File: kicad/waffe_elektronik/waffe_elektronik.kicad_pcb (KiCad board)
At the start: 4 copper layers, 59.6 x 51 mm, 81 parts, among them J1 WS2812 HP-Streifen, J2 GX16 7-polig, J3 USB-C (Flashen + Laden), J4 OLED I²C (Qwiic), J5 Drehgeber, J6 TSOP 6 (Waffe), J7 TF-018, M1 Vibromotor, Q1 AO3400A, Q2 AO3400A, Q3 FS8205A, SW1 Taster, SW2 Taster, SW3 RESET, SW4 BOOT, U1 MT3608, U12 USBLC6-2SC6, U14 GD5F1GQ5UEYIGR, U15 DW01A, U2 AMS1117-3.3, U3 MCP73831, U4 ESP32-S3-WROOM-1-N16R8, U5 74HCT125, U6 MAX98357A

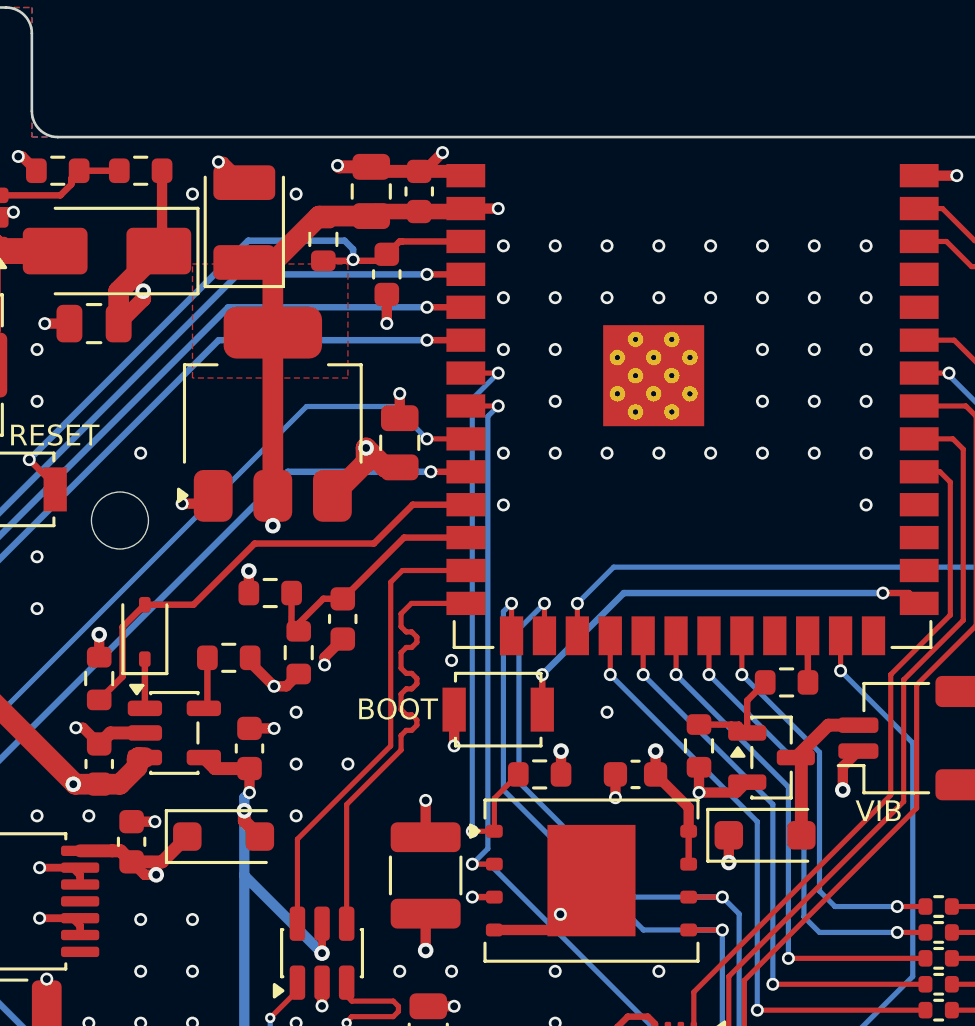
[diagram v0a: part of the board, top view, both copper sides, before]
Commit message: Platine: günstigere JLC-Teile, Option ESP32-S3-WROOM-1U mit externer Antenne
- Flash ZD35Q1GC-IB, Kondensatoren/Dioden/Widerstände auf Basic-Teile und 0402, Layout angepasst
- WROOM-1U auf demselben Footprint: eigene JLCPCB-BOM/CPL (Modulmitte 3,15 mm versetzt),
  Mouser-Option mit Pigtail RP-SMA/U.FL und Knick-Stabantenne, 3D-Modell des 1U
- Gerber, BOM, CPL, Renders und Bestelllisten neu erzeugt

Co-Authored-By: Claude Opus 5.5 <noreply@anthropic.com>
Claude-Session: https://claude.ai/code/session_01KkZzubjLKyW9odUwvmxTog
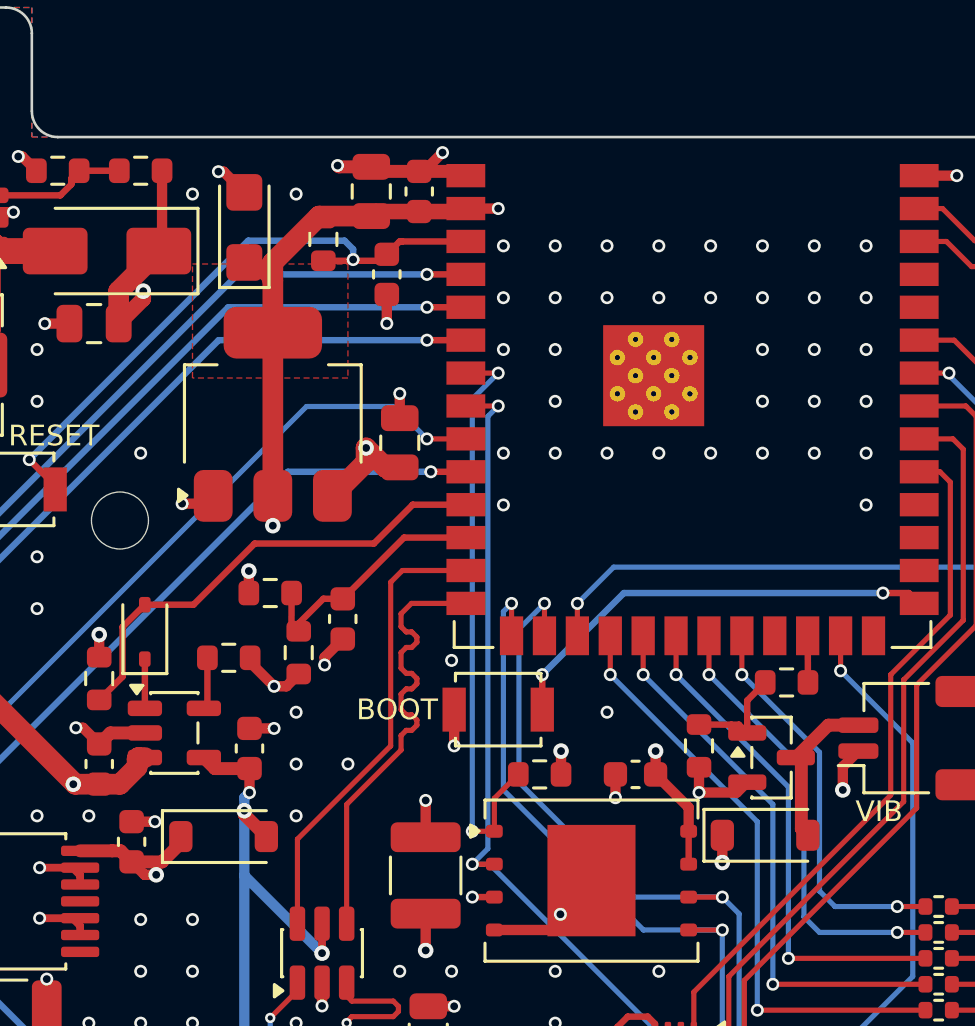
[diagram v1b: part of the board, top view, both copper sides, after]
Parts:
- C3: footprint Capacitor_Tantalum_SMD:CP_EIA-3528-21_Kemet-B -> Capacitor_Tantalum_SMD:CP_EIA-3216-18_Kemet-A
- D1, D4: value SS14 -> B5819W; footprint Diode_SMD:D_SOD-123F -> Diode_SMD:D_SOD-123
- D5: value BAT54WS -> 1N5819WS
- U14: value GD5F1GQ5UEYIGR -> ZD35Q1GC-IB
- moved C3 0.19 mm to (25.2, 3.49)

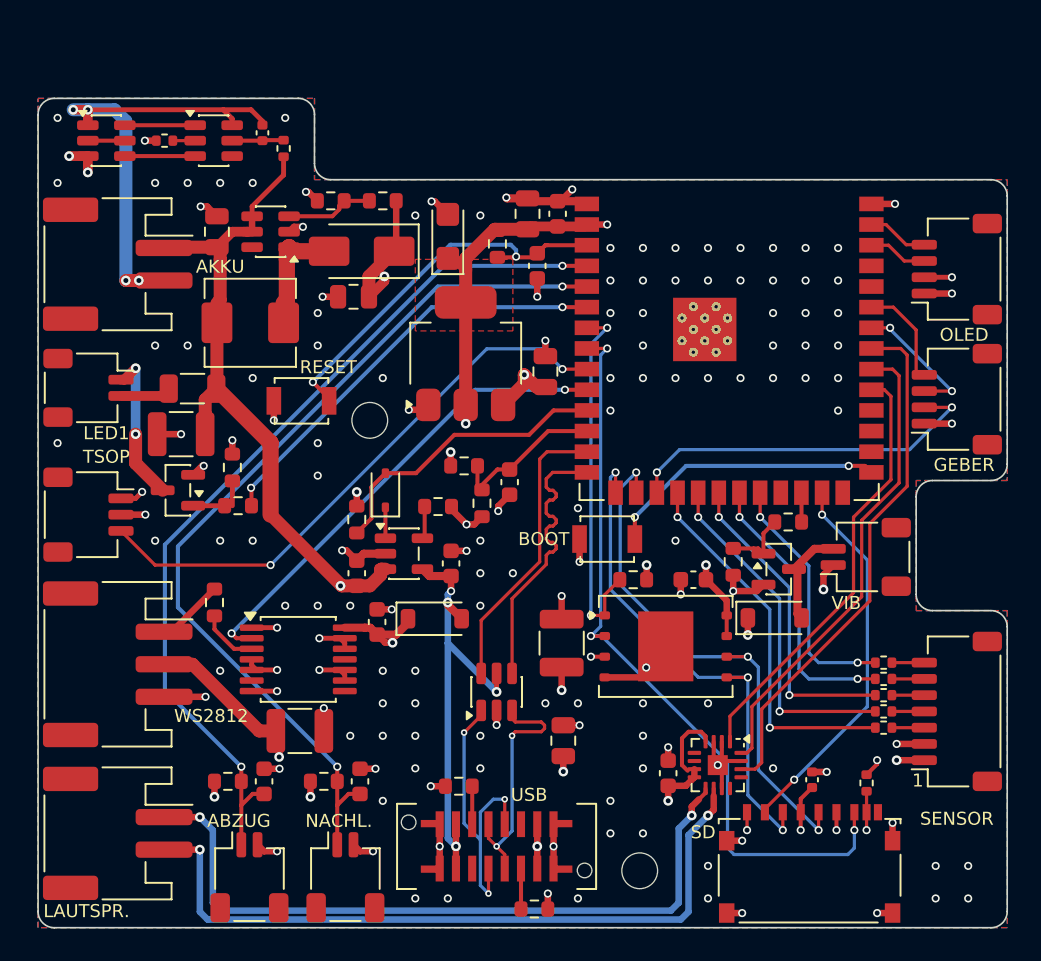
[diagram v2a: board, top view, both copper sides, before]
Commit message: Platine: microSD-Slot gedreht, Ein/Aus über den Drehgeber-Taster, R7 12 Ω, 10 µF am Slot
- J7: Karte wird auf der Kontaktseite eingesteckt (Datenblatt TF-018) -> Slot gedreht, Kontakte und
  Öffnung an der Unterkante, SD-Leitungen neu verlegt
- Soft-Power: Q4 (AO3401A) trennt den Akku von BAT_SW, Taster an J5.2 schaltet über D6 (BAT54CW) ein,
  IO21 hält über Q5, IO9 liest den Taster; Lasche oben links 18,6 x 9 mm mit den neuen Teilen,
  Leitungen auf B.Cu über die Oberkante, Akku-Plus über In2
- R7 12 Ω (C17913), C28 10 µF an der microSD-Versorgung
- Gerber, BOM/CPL (alle Varianten), Mouser-BOM, Renders und Doku neu

Co-Authored-By: Claude Opus 5.5 <noreply@anthropic.com>
Claude-Session: https://claude.ai/code/session_01KkZzubjLKyW9odUwvmxTog
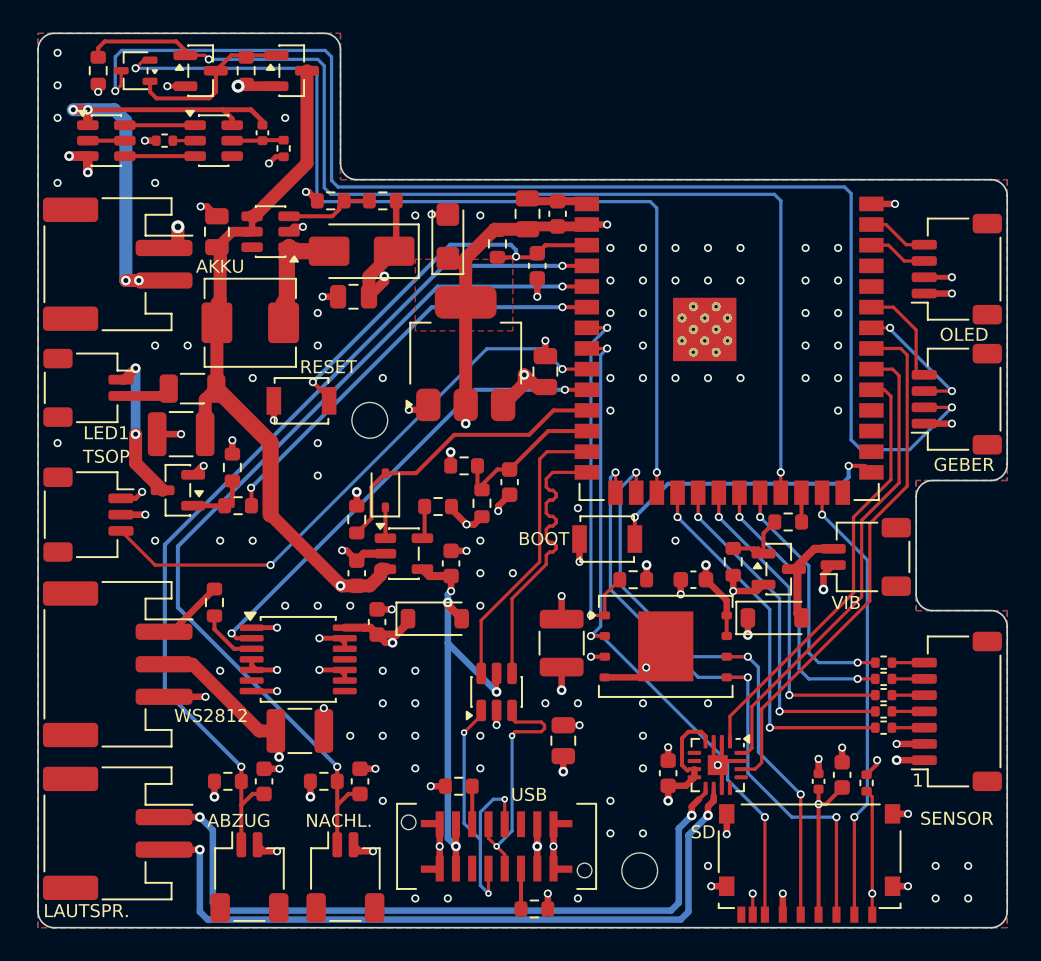
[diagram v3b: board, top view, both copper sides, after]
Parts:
- added C28: 10u, Capacitor_SMD:C_0603_1608Metric, F.Cu at (49.5, 36.6)
- added D6: BAT54CW, Package_TO_SOT_SMD:SOT-323_SC-70, F.Cu at (6.00, -6.70)
- added Q4: AO3401A, Package_TO_SOT_SMD:SOT-23, F.Cu at (15.6, -6.70)
- added Q5: AO3400A, Package_TO_SOT_SMD:SOT-23, F.Cu at (10.0, -6.70)
- added R38: 100k, Resistor_SMD:R_0603_1608Metric, F.Cu at (12.8, -6.70)
- added R40: 100k, Resistor_SMD:R_0603_1608Metric, F.Cu at (3.70, -6.70)
- R7: value 10 -> 12
- moved C26 0.41 mm to (48.0, 37.0)
- moved J7 0.10 mm to (47.5, 42.1), turned to 0 degrees
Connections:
- C19 pad 1: BAT_P -> BAT_SW
- C5 pad 1: BAT_P -> BAT_SW
- C7 pad 1: BAT_P -> BAT_SW
- J5 pad 2: ENC_SW -> PWR_KEY
- L1 pad 1: BAT_P -> BAT_SW
- R3 pad 1: BAT_P -> BAT_SW
- R7 pad 1: BAT_P -> BAT_SW
- U1 pad 4: BAT_P -> BAT_SW
- U1 pad 5: BAT_P -> BAT_SW
- U3 pad 3: BAT_P -> BAT_SW
- U4 pad 23: unconnected-(U4-IO21-Pad23) -> PWR_HOLD
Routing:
- net PWR_KEY: track 0.00 -> 81.4 mm, vias 0 -> 2
- net PWR_HOLD: track 0.00 -> 69.3 mm, vias 0 -> 2
- net BAT_SW: track 0.00 -> 54.2 mm, vias 0 -> 2
- net ENC_SW: track 22.8 -> 58.5 mm
- net BAT_P: track 51.5 -> 19.6 mm, vias 2 -> 3
- net Net-(Q4-G): track 0.00 -> 10.6 mm
- net SPI_MOSI: track 32.0 -> 39.0 mm
- net SPI_MISO: track 47.4 -> 42.2 mm
- net 3V3_MCU: track 173.2 -> 178.2 mm
- net SD_CS: track 23.4 -> 27.4 mm
- net SPI_CLK: track 33.1 -> 36.8 mm
- net SD_DAT12: track 15.2 -> 17.5 mm
- net GND: vias 153 -> 146
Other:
- board size 59.6 x 51 mm -> 59.6 x 55 mm

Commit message: Platine: IP5306 (2 A Laden + 5 V) statt MT3608/MCP73831, Ein/Aus über KEY, eigener I²C-Bus
Co-Authored-By: Claude Opus 5.5 <noreply@anthropic.com>
Claude-Session: https://claude.ai/code/session_01KkZzubjLKyW9odUwvmxTog
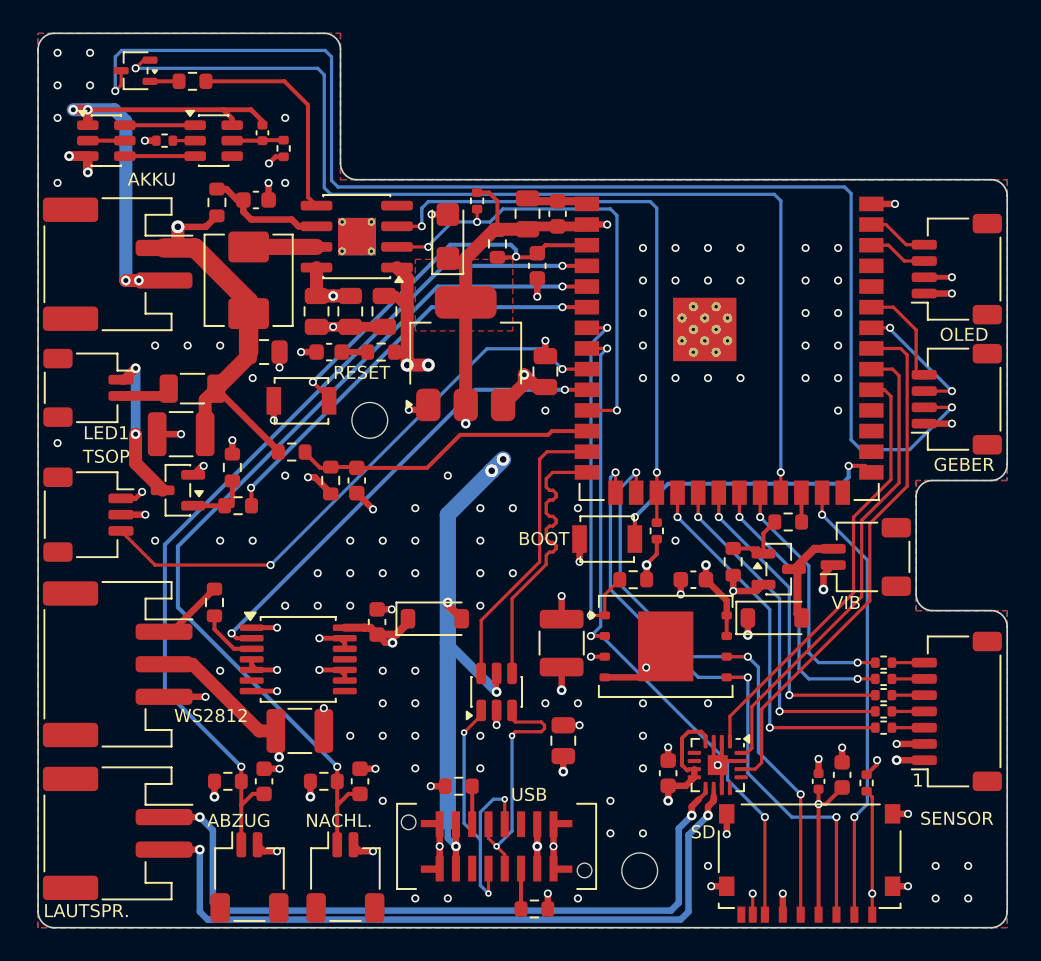
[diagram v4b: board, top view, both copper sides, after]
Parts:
- removed D3: SS34, Diode_SMD:D_SMA
- removed D5: 1N5819WS, Diode_SMD:D_SOD-323
- removed Q4: AO3401A, Package_TO_SOT_SMD:SOT-23
- removed Q5: AO3400A, Package_TO_SOT_SMD:SOT-23
- removed R25: 10k, Resistor_SMD:R_0603_1608Metric
- removed U3: MCP73831, Package_TO_SOT_SMD:SOT-23-5
- added C29: 10u, Capacitor_SMD:C_0603_1608Metric, F.Cu at (17.9, 10.6)
- added C30: 22u, Capacitor_SMD:C_0805_2012Metric, F.Cu at (19.2, 8.10)
- C4: value 1u -> 10u; footprint Capacitor_SMD:C_0603_1608Metric -> Capacitor_SMD:C_0805_2012Metric
- C5: value 1u -> 22u
- L1: value 10u -> 1u
- R1: value 2k -> 2
- R2: value 10k -> 1
- R24: value 75k -> 10k
- R3, R4: value 100k -> 1M
- R38, R40: value 100k -> 4.7k; footprint Resistor_SMD:R_0603_1608Metric -> Resistor_SMD:R_0402_1005Metric
- U1: value MT3608 -> IP5306-I2C; footprint Package_TO_SOT_SMD:SOT-23-6 -> Package_SO:HSOP-8-1EP_3.9x4.9mm_P1.27mm_EP2.3x2.3mm_ThermalVias
- moved R38 37.9 mm to (38.0, 21.6), turned to 90 degrees
- moved R40 24.6 mm to (27.0, 1.30)
- moved C5 23.8 mm to (13.4, 1.25), turned to 0 degrees
- moved R2 21.3 mm to (11.0, 1.40)
- moved C4 16.0 mm to (21.3, 8.10), turned to -90 degrees
- moved R24 13.8 mm to (9.50, -6.05)
- moved R3 10.6 mm to (15.6, 16.8)
- moved R1 10.1 mm to (21.1, 10.6), turned to 180 degrees
- moved R4 9.40 mm to (18.0, 18.5)
- moved C6 9.40 mm to (19.6, 18.5)
- moved C19 7.95 mm to (13.9, 10.6), turned to 0 degrees
- moved U1 5.31 mm to (19.6, 3.50)
- moved L1 2.62 mm to (12.9, 6.18), turned to -90 degrees
- moved C20 2.45 mm to (17.1, 8.10), turned to -90 degrees
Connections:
- C19 pad 1: BAT_SW -> BAT_P
- C5 pad 1: BAT_SW -> Net-(U1-BAT)
- C7 pad 1: BAT_SW -> BAT_P
- D6 pad 1: Net-(Q4-G) -> Net-(D6-Pad1)
- L1 pad 1: BAT_SW -> Net-(U1-SW)
- L1 pad 2: Net-(D3-A) -> BAT_P
- R1 pad 1: Net-(U3-PROG) -> VBUS_NATIVE
- R1 pad 2: GND -> Net-(C29-Pad1)
- R2 pad 1: 3V3_MCU -> Net-(U1-BAT)
- R2 pad 2: CHRG_STAT -> BAT_P
- R24 pad 1: 5V_PERIPH -> IP_KEY
- R24 pad 2: Net-(U1-FB) -> Net-(D6-Pad1)
- R3 pad 1: BAT_SW -> BAT_P
- R38 pad 1: Net-(Q4-G) -> 3V3_MCU
- R38 pad 2: BAT_P -> IP_SDA
- R40 pad 1: PWR_HOLD -> 3V3_MCU
- R40 pad 2: GND -> IP_SCL
- R7 pad 1: BAT_SW -> BAT_P
- U1 pad 1: Net-(D3-A) -> VBUS_NATIVE
- U1 pad 2: GND -> IP_SCL
- U1 pad 3: Net-(U1-FB) -> IP_SDA
- U1 pad 4: BAT_SW -> unconnected-(U1-LED3-Pad4)
- U1 pad 5: BAT_SW -> IP_KEY
- U1 pad 6: unconnected-(U1-NC-Pad6) -> Net-(U1-BAT)
- U4 pad 11: CHRG_STAT -> IP_SCL
- U4 pad 17: ENC_SW -> IP_SDA
- U4 pad 23: PWR_HOLD -> ENC_SW
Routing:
- net PWR_HOLD: track 69.3 -> 0.00 mm, vias 2 -> 0
- net BAT_SW: track 54.2 -> 0.00 mm, vias 2 -> 0
- net IP_SDA: track 0.00 -> 36.8 mm, vias 0 -> 2
- net IP_SCL: track 0.00 -> 29.3 mm, vias 0 -> 3
- net VBUS_NATIVE: track 41.6 -> 69.4 mm, vias 5 -> 8
- net CHRG_STAT: track 18.4 -> 0.00 mm
- net BAT_P: track 19.6 -> 35.5 mm, vias 3 -> 2
- net IP_KEY: track 0.00 -> 13.3 mm
- net Net-(Q4-G): track 10.6 -> 0.00 mm
- net ADC_BATT: track 9.72 -> 18.7 mm
- net ENC_SW: track 58.5 -> 66.2 mm
- net Net-(U1-BAT): track 0.00 -> 7.50 mm
- net Net-(D3-A): track 5.56 -> 0.00 mm
- net Net-(U1-FB): track 5.46 -> 0.00 mm
- net 3V3_MCU: track 178.2 -> 182.4 mm, vias 13 -> 12
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
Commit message: Platine: Stecker zusammengelegt, Basic-Teile, MOSFET-Pegelwandler, Flash optional, Kabel-3V3 über 10 Ω, breitere 5-V- und Akku-Wege
Co-Authored-By: Claude Opus 5.5 <noreply@anthropic.com>
Claude-Session: https://claude.ai/code/session_01KkZzubjLKyW9odUwvmxTog
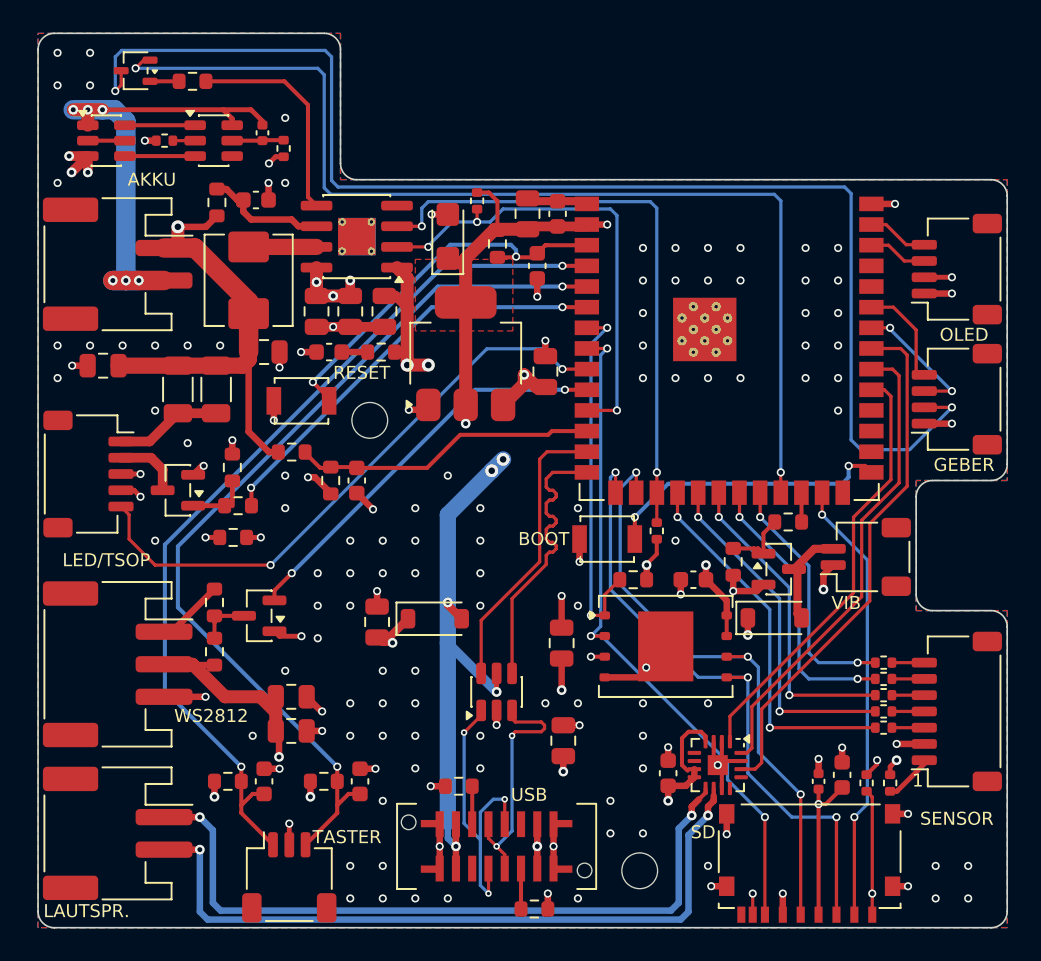
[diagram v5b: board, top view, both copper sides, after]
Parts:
- removed C21: 100n, Capacitor_SMD:C_0603_1608Metric
- removed LED1: TSAL6100, Connector_JST:JST_SH_SM02B-SRSS-TB_1x02-1MP_P1.00mm_Horizontal
- removed SW1, SW2: Taster, Connector_JST:JST_SH_SM02B-SRSS-TB_1x02-1MP_P1.00mm_Horizontal
- removed U5: 74HCT125, Package_SO:TSSOP-14_4.4x5mm_P0.65mm
- added C31: 22u, Capacitor_SMD:C_0805_2012Metric, F.Cu at (20.9, 27.2)
- added C32: 22u, Capacitor_SMD:C_0805_2012Metric, F.Cu at (15.6, 31.8)
- added J8: Abzug + Nachladen, Connector_JST:JST_SH_SM03B-SRSS-TB_1x03-1MP_P1.00mm_Horizontal, F.Cu at (15.4, 42.9)
- added Q4: 2N7002, Package_TO_SOT_SMD:SOT-23, F.Cu at (13.6, 26.8)
- added R25: 1k, Resistor_SMD:R_0603_1608Metric, F.Cu at (10.8, 29.0)
- added R35: 10, Resistor_SMD:R_0402_1005Metric, F.Cu at (52.4, 37.1)
- added R36: 10, Resistor_SMD:R_0603_1608Metric, F.Cu at (12.0, 22.0)
- added R8: 22, Resistor_SMD:R_1206_3216Metric, F.Cu at (10.9, 12.9)
- C1, C10, C7: value 100u -> 22u; footprint Capacitor_SMD:C_1210_3225Metric -> Capacitor_SMD:C_0805_2012Metric
- J6: value TSOP 6 (Waffe) -> IR-LED + TSOP 6; footprint Connector_JST:JST_SH_SM03B-SRSS-TB_1x03-1MP_P1.00mm_Horizontal -> Connector_JST:JST_SH_SM05B-SRSS-TB_1x05-1MP_P1.00mm_Horizontal
- R7: value 12 -> 22
- moved C7 6.39 mm to (4.00, 11.4)
- moved J6 2.50 mm to (3.10, 18.1)
- moved R7 0.90 mm to (8.60, 12.9), turned to -90 degrees
- moved C10 0.53 mm to (15.6, 33.9)
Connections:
- J2 pad 1: 3V3_MCU -> 3V3_WESTE
- J6 pad 1: 3V3_MCU -> IR_LED_A
- J6 pad 2: GND -> IR_LED_K
- J6 pad 3: TSOP6_OUT -> GND
- Q1 pad 3: Net-(LED1-K) -> IR_LED_K
- R7 pad 2: Net-(LED1-A) -> IR_LED_A
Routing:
- net Net-(LED1-K): track 9.38 -> 0.00 mm, vias 2 -> 0
- net GND: track 82.3 -> 73.6 mm, vias 146 -> 148
- net 3V3_J6: track 0.00 -> 7.28 mm, vias 0 -> 2
- net IR_LED_A: track 0.00 -> 6.57 mm
- net 5V_PERIPH: track 121.3 -> 127.0 mm, vias 9 -> 11
- net WS2812_DIN_3V3: track 29.4 -> 24.9 mm
- net BAT_P: track 35.5 -> 39.8 mm
- net IR_LED_K: track 0.00 -> 4.14 mm
- net Net-(LED1-A): track 3.12 -> 0.00 mm
- net 3V3_MCU: track 182.4 -> 179.4 mm, vias 12 -> 13
- net 3V3_WESTE: track 0.00 -> 3.03 mm
- net BAT_N: track 30.8 -> 33.3 mm, vias 4 -> 6
- net TSOP6_OUT: track 35.5 -> 37.0 mm
- net TRIGGER: track 55.1 -> 55.9 mm
- net RELOAD: track 55.9 -> 56.7 mm
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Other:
- board text added: "LED/TSOP"
- board text added: "TASTER"
- board text removed: "ABZUG"
- board text removed: "LED1"
- board text removed: "NACHL."
- board text removed: "TSOP"
